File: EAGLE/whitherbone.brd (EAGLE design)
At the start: 86.4 x 54.6 mm, 222 parts, among them IC10 TXS0108ERGYR, IC11 TXS0108ERGYR, IC12 TPS2051BDGN, IC13 SN74AUC1G74, IC14 TPD4S012DRY, IC15 TPD4S012DRY, IC17 SN74LVC2G241DCUR, IC18 TL1963ADCQR, IC19 AP2112K-1.8TRG1 3.3V, IC2 SN74LVC1G07DCK, IC4 7805T, IC7 IP4283CZ10-TBR, IC8 IP4283CZ10-TBR, IC9 TDA19988BHN/C1,557, J1 1-1747981-1, Q2 32.768kHz, Q4 24 MHz, T1 BSS138W-7-F, T3 BSS138W-7-F, T4 BSS138W-7-F, U1 OSD3358-512M-BSM, U2 A3967SLBTR, X2 SCHA5B0200, X4 10118192-0001LF

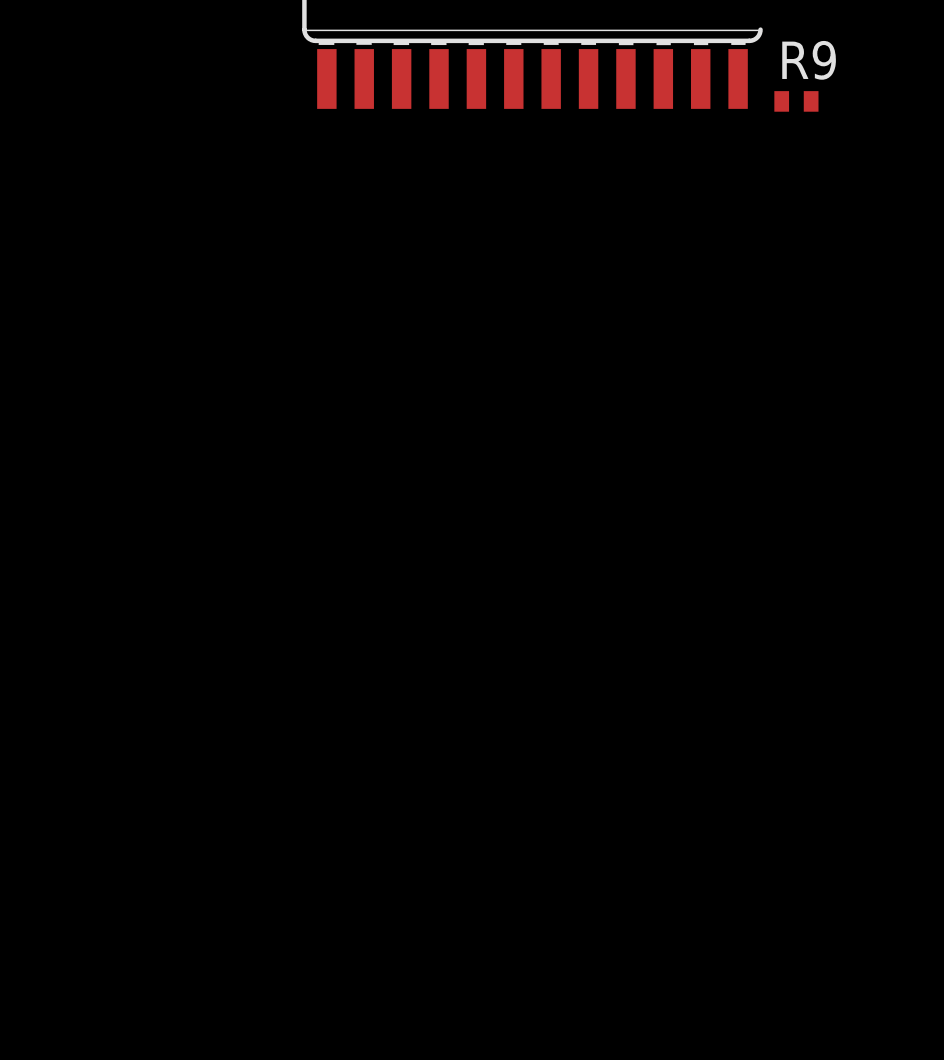
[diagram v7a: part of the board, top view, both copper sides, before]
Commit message: Started motor driver
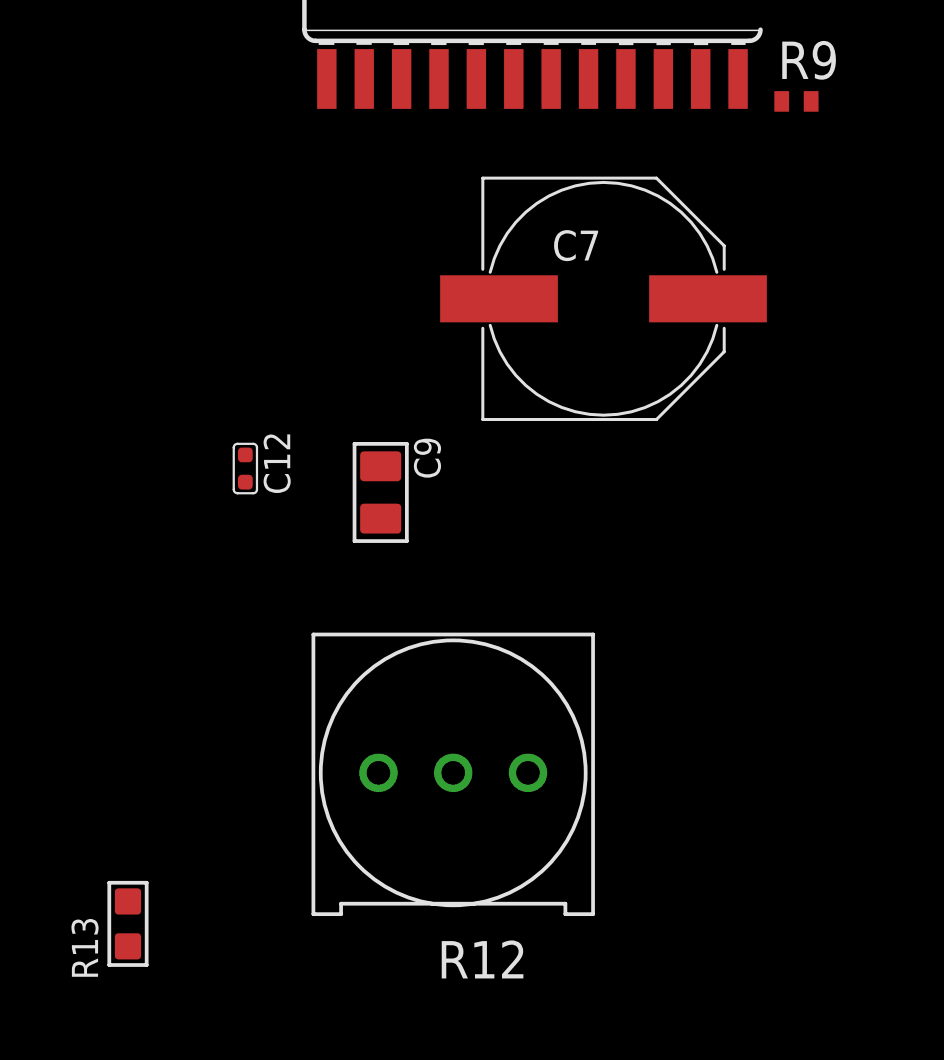
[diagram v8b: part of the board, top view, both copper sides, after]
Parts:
- added C12: 1uF,10V, Seeed-Capacitor:C0402
- added C7: 47uF,50V, resistor:PANASONIC_F
- added C9: 100nF,50V, Seeed-Capacitor:C0805
- added R12: 10K, Seeed-Resistor:ADJR3-9.5X9.5X10.5MM
- added R13: 2K, Seeed-Resistor:R0603
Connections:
- removed net VCC: U2.14
- new net 12VDC: C7.+, IC4.1, X12.IN
- new net N$31: R12.1, R13.2
- net GND: now also C7.-, R13.1
- net N$10: now also R12.3, U2.1; no longer IC4.1, X12.IN
- net VDD_5V: now also R12.2, U2.14
